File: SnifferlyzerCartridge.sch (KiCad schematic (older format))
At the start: 3 parts, among them J1 Cartridge Connector, U1 W25Q128

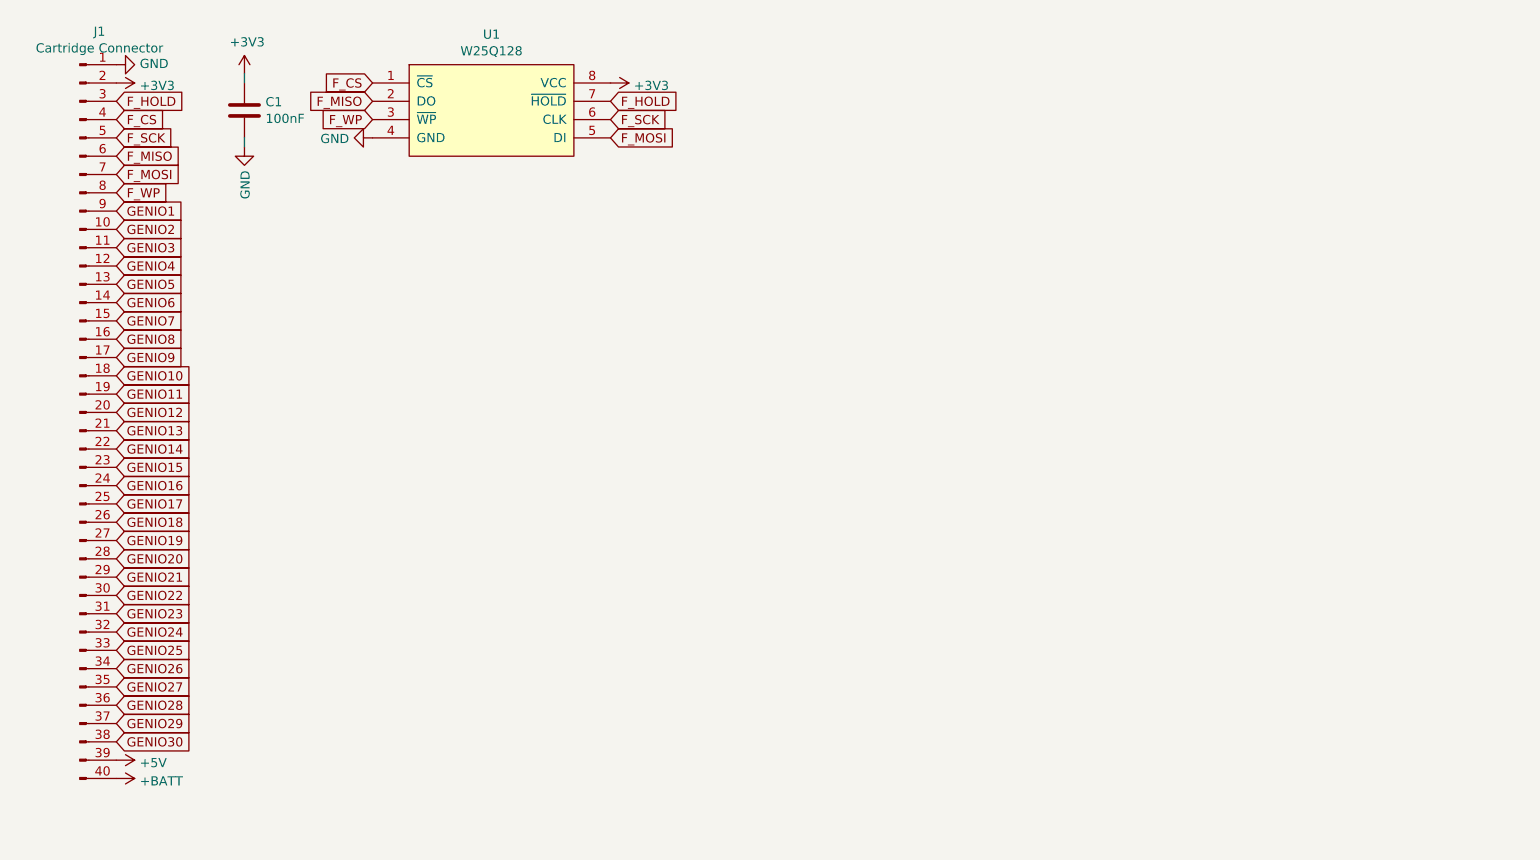
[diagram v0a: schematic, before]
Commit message: First design of the Snifferlyzer cartridge
Also updated:
- README
- Render image
- .gitignore
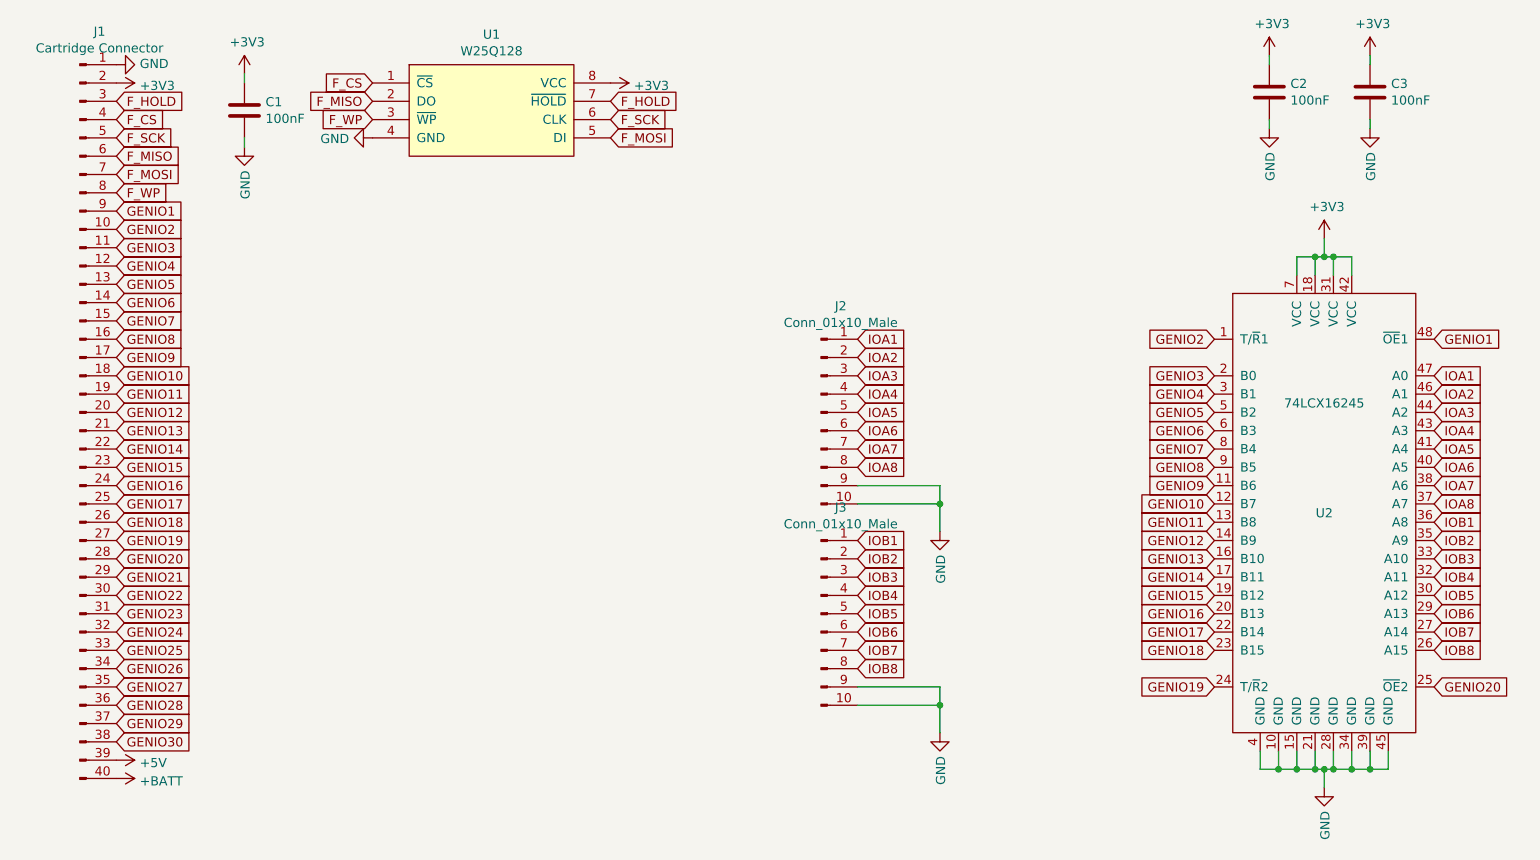
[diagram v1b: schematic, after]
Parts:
- added C2, C3: 100nF, Capacitors_SMD:C_0805_HandSoldering, symbol device:C
- added J2, J3: Conn_01x10_Male, Pin_Headers:Pin_Header_Angled_1x10_Pitch2.54mm, symbol Connector:Conn_01x10_Male
- added U2: 74LCX16245, Housings_SSOP:TSSOP-48_6.1x12.5mm_Pitch0.5mm, symbol SuperconCartridge:74LCX16245
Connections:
- net +3V3: now also C2.1, C3.1, U2.18 (VCC), U2.31 (VCC), U2.42 (VCC), U2.7 (VCC)
- net GENIO1: now also U2.48 (~OE~1)
- net GENIO10: now also U2.12 (B7)
- net GENIO11: now also U2.13 (B8)
- net GENIO12: now also U2.14 (B9)
- net GENIO13: now also U2.16 (B10)
- net GENIO14: now also U2.17 (B11)
- net GENIO15: now also U2.19 (B12)
- net GENIO16: now also U2.20 (B13)
- net GENIO17: now also U2.22 (B14)
- net GENIO18: now also U2.23 (B15)
- net GENIO19: now also U2.24 (T/~R~2)
- net GENIO2: now also U2.1 (T/~R~1)
- net GENIO20: now also U2.25 (~OE~2)
- net GENIO3: now also U2.2 (B0)
- net GENIO4: now also U2.3 (B1)
- net GENIO5: now also U2.5 (B2)
- net GENIO6: now also U2.6 (B3)
- net GENIO7: now also U2.8 (B4)
- net GENIO8: now also U2.9 (B5)
- net GENIO9: now also U2.11 (B6)
- net GND: now also C2.2, C3.2, J2.10 (Pin_10), J2.9 (Pin_9), J3.10 (Pin_10), J3.9 (Pin_9), U2.10 (GND), U2.15 (GND), U2.21 (GND), U2.28 (GND), U2.34 (GND), U2.39 (GND), U2.4 (GND), U2.45 (GND)
- new net IOA1: J2.1 (Pin_1), U2.47 (A0)
- new net IOA2: J2.2 (Pin_2), U2.46 (A1)
- new net IOA3: J2.3 (Pin_3), U2.44 (A2)
- new net IOA4: J2.4 (Pin_4), U2.43 (A3)
- new net IOA5: J2.5 (Pin_5), U2.41 (A4)
- new net IOA6: J2.6 (Pin_6), U2.40 (A5)
- new net IOA7: J2.7 (Pin_7), U2.38 (A6)
- new net IOA8: J2.8 (Pin_8), U2.37 (A7)
- new net IOB1: J3.1 (Pin_1), U2.36 (A8)
- new net IOB2: J3.2 (Pin_2), U2.35 (A9)
- new net IOB3: J3.3 (Pin_3), U2.33 (A10)
- new net IOB4: J3.4 (Pin_4), U2.32 (A11)
- new net IOB5: J3.5 (Pin_5), U2.30 (A12)
- new net IOB6: J3.6 (Pin_6), U2.29 (A13)
- new net IOB7: J3.7 (Pin_7), U2.27 (A14)
- new net IOB8: J3.8 (Pin_8), U2.26 (A15)
